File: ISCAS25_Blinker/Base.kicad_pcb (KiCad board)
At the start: 2 copper layers, 85 x 35 mm, 6 parts

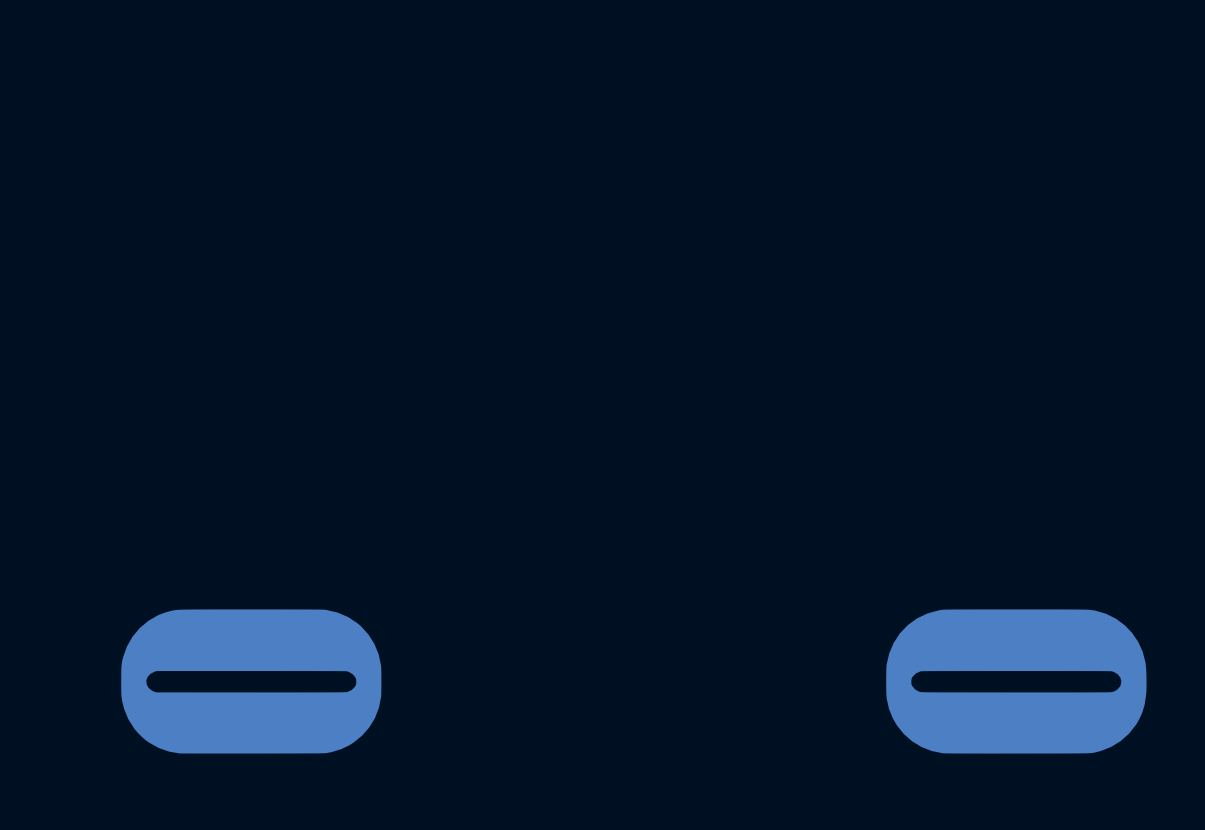
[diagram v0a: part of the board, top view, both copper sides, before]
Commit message: Schematic done
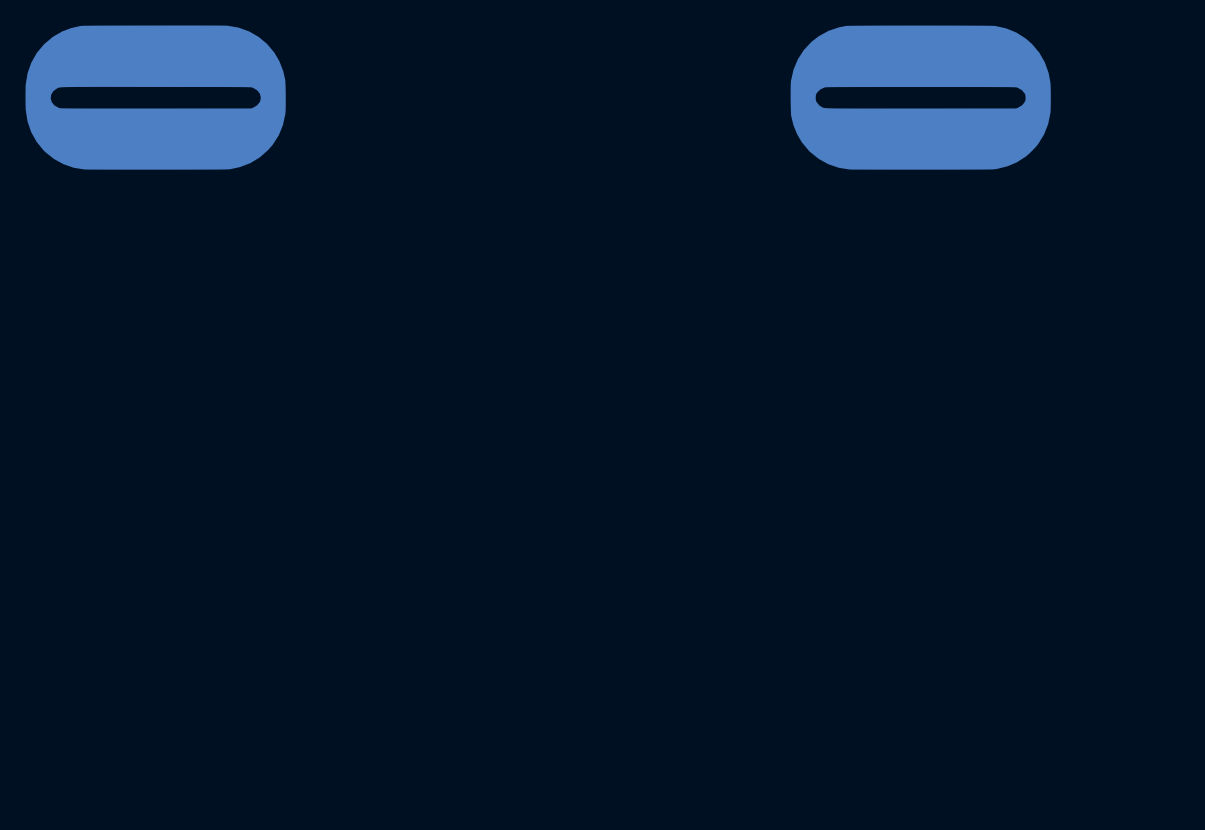
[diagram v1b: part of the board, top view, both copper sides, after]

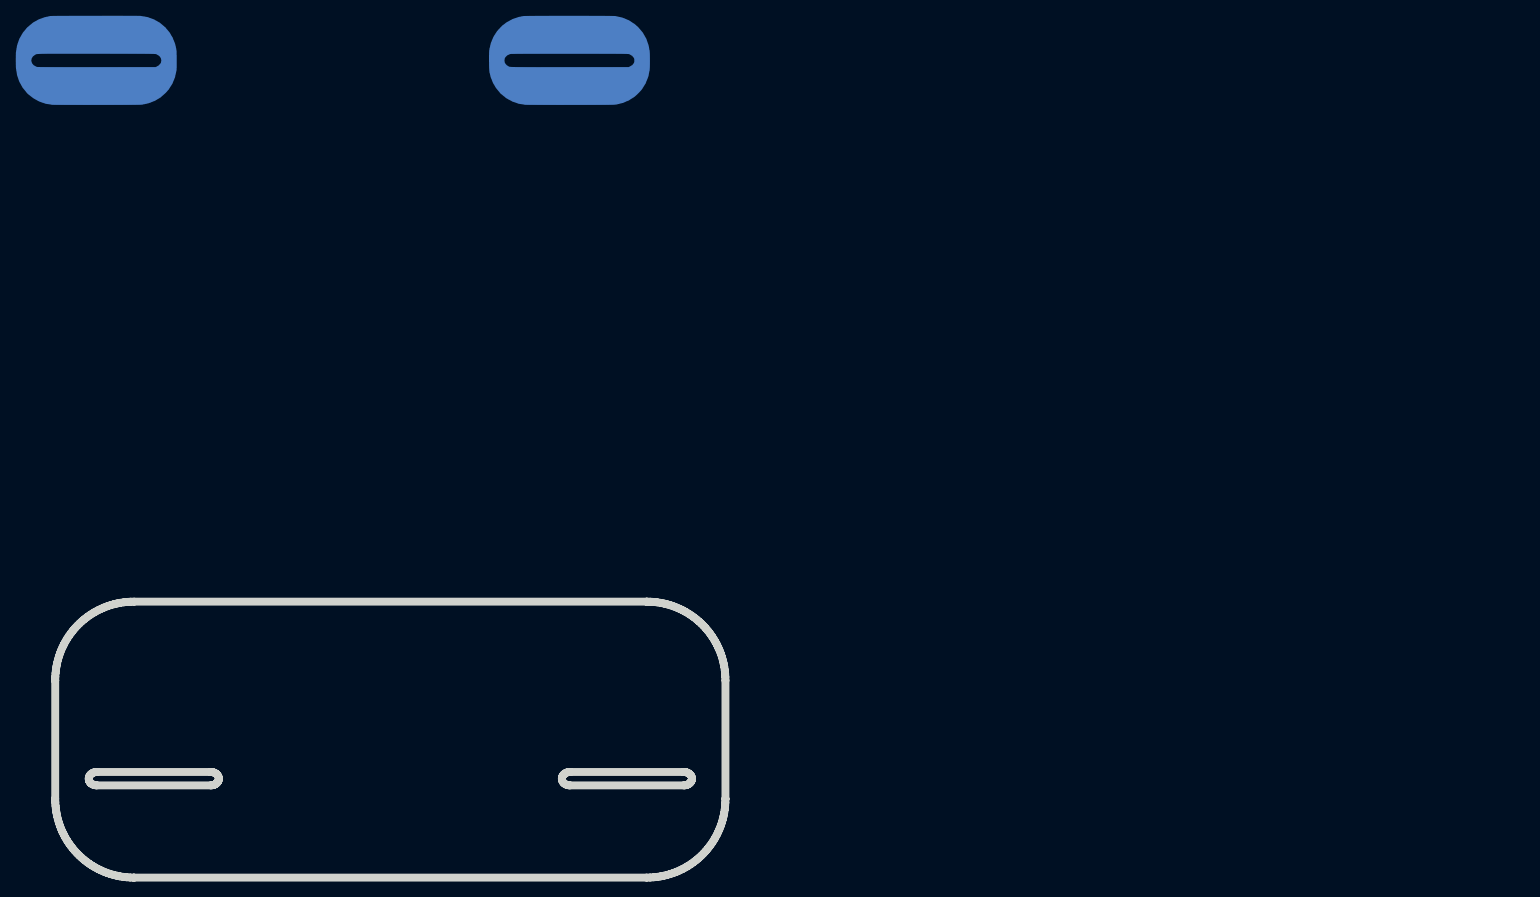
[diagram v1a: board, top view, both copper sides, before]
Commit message: Fixed aux PCBs
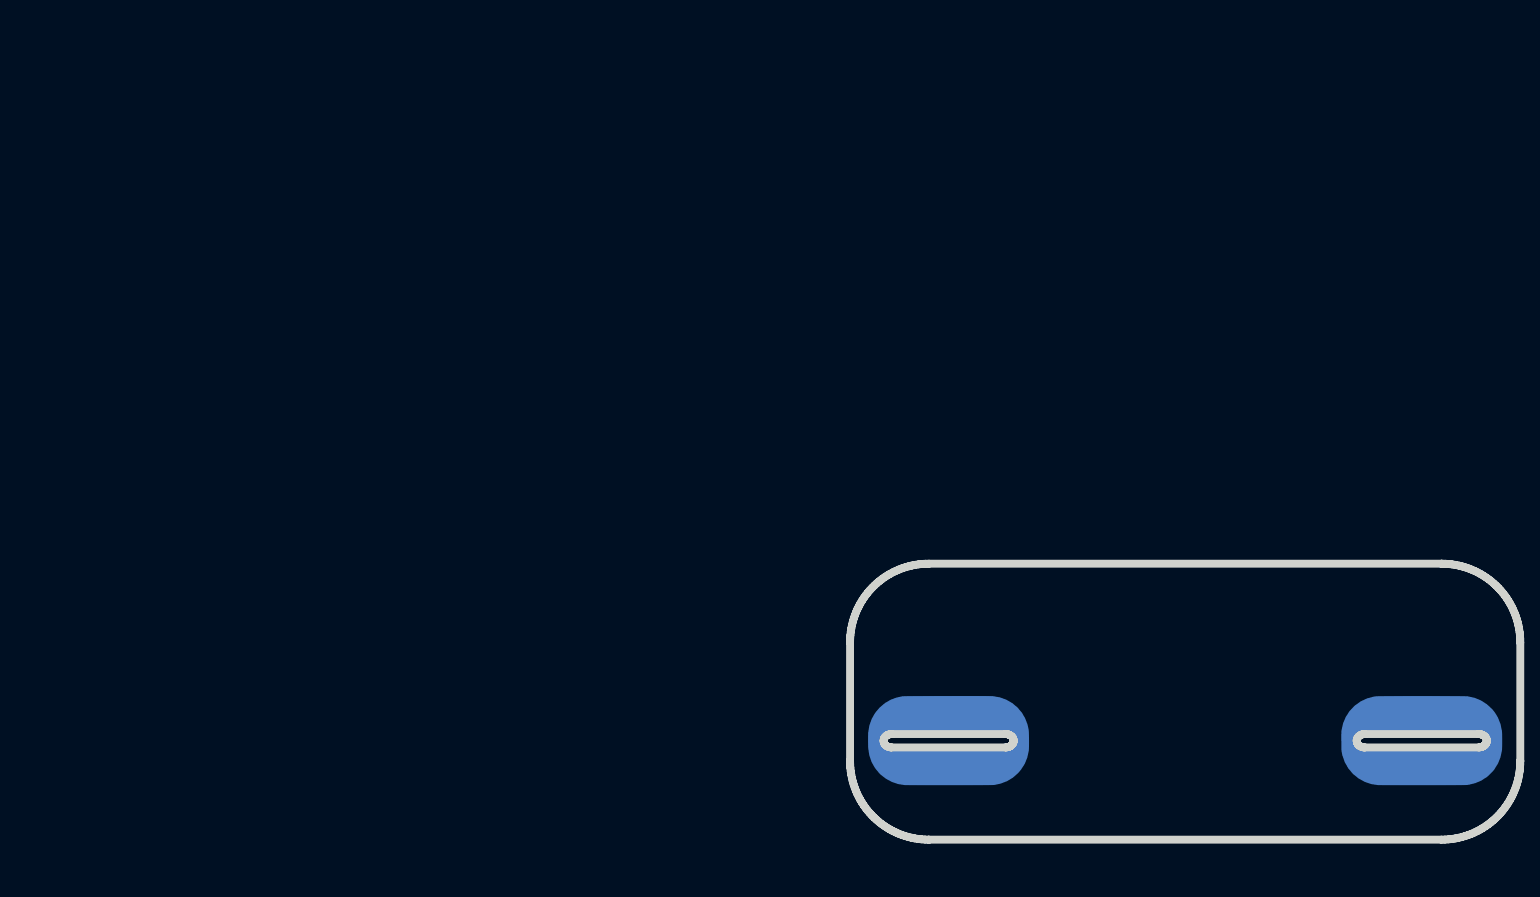
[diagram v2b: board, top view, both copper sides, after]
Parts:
- ? (x4): moved to F.Cu
- moved ? 138.3 mm to (108.1, 86.3) (x6)
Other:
- outline, holes or cut-outs redrawn
